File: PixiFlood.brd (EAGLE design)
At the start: 43 x 46 mm, 37 parts, among them IC1 TC7W04FP-0.65, IC2 WS2811S, IC3 78L05Z, U1 PT4115B89E, U2 PT4115B89E, U3 PT4115B89E, X1 22-23-2031, X2 22-23-2031

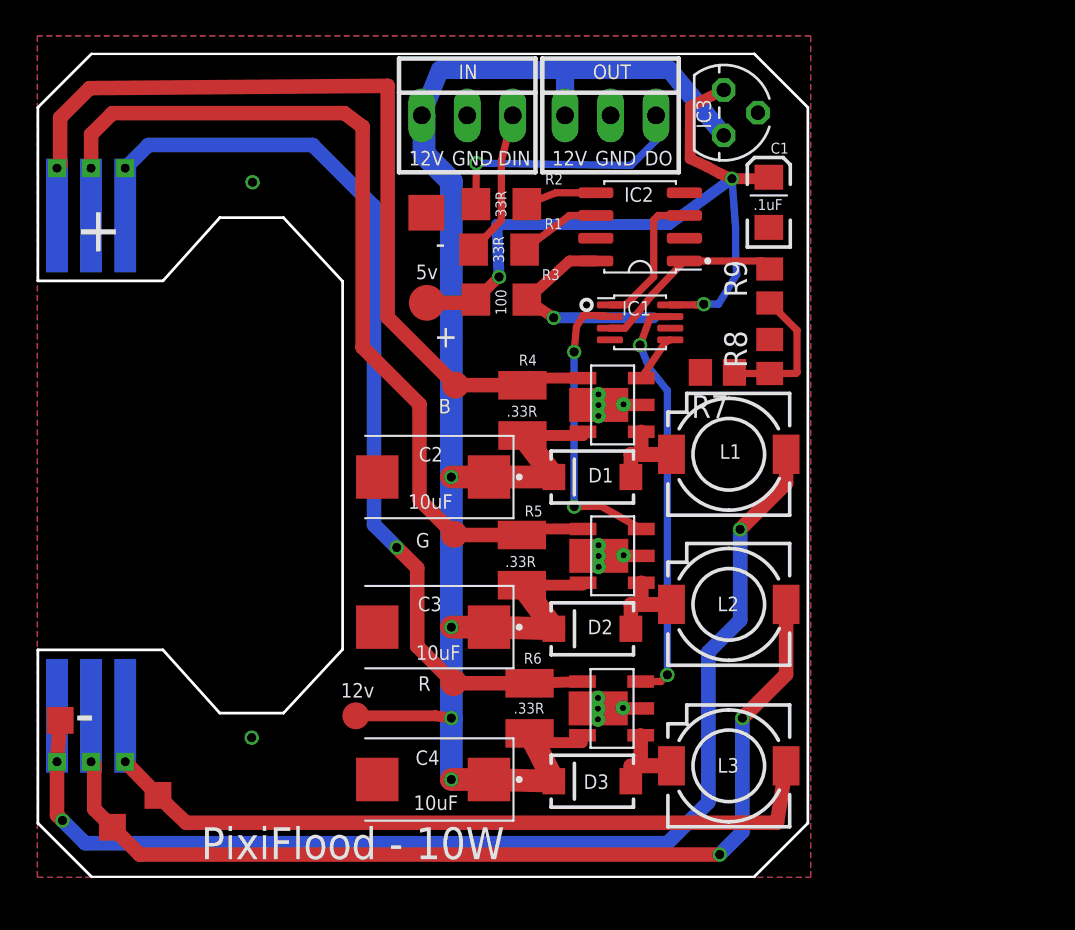
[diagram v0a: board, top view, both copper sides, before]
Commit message: Reworked layout
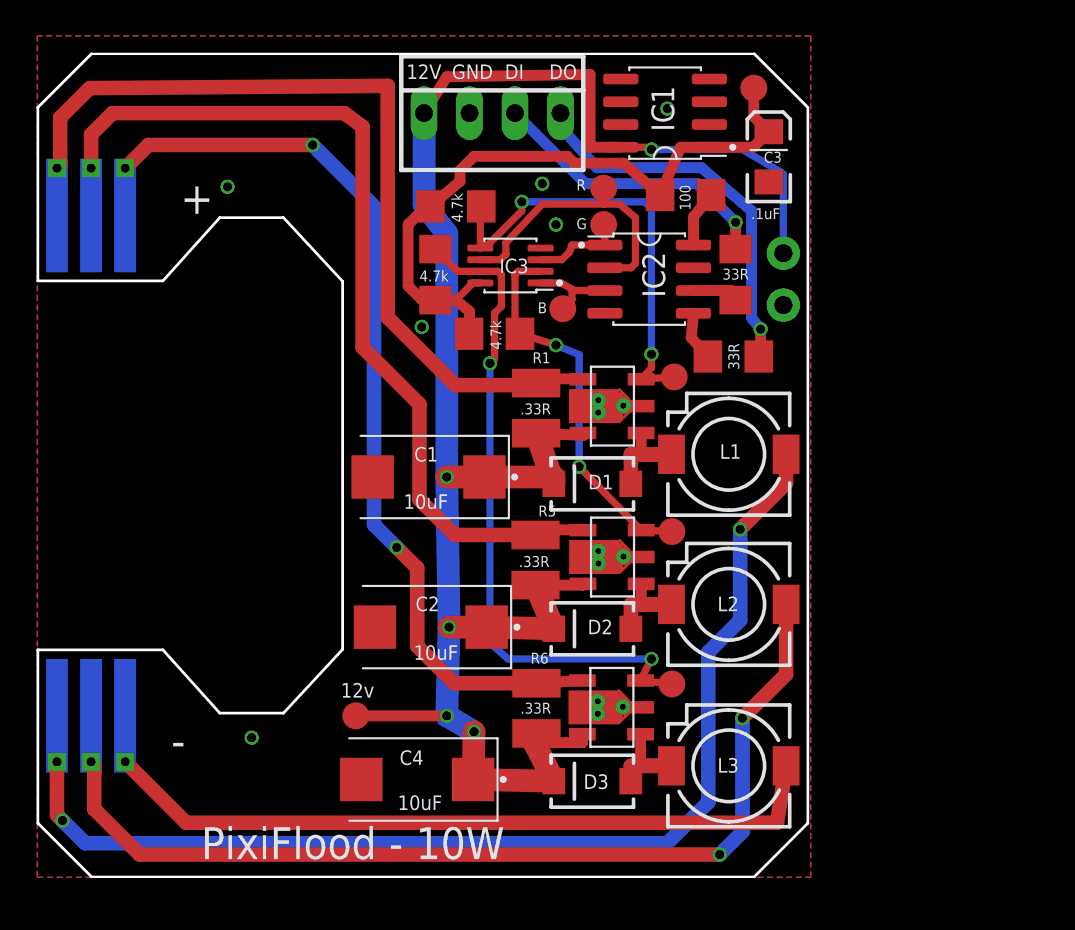
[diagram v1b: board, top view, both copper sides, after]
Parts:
- removed TP8: TPSQTP15SQ, testpad:TP15SQ
- removed X2: 22-23-2031, MyLibrary:22-23-2031
- added JP1: M02NO_SILK_LOCK, connectors:1X02_LOCK_NO_SILK
- C1: value .1uF -> 10uF; device capacitors:EIA3216 -> capacitors:VISHAY-CASE-D
- C3: value 10uF -> .1uF; device capacitors:VISHAY-CASE-D -> capacitors:EIA3216
- IC1: value TC7W04FP-0.65 -> 78L05SMD; device logic:SSOP8-0.65P -> regulators:SO08
- IC2: device drivers:WS2811S -> drivers:SO08
- IC3: value 78L05Z -> TC7W04FP-0.65; device linear:TO92 -> logic:SSOP8-0.65P
- R1: value 33R -> .33R; device rcl:R1206 -> resistor:R1210
- R3: value 100 -> 33R
- R4: value .33R -> 100; device resistor:R1210 -> rcl:R1206
- R7, R8, R9: value 4.7K -> 4.7k; device rcl:R0805 -> rcl:R1206
- TP1: value TPSQTP20R -> TPSQTP15R; device testpad:TP20R -> testpad:TP15R
- TP2: value TPSQTP20SQ -> TPSQTP15R; device testpad:TP20SQ -> testpad:TP15R
- TP4, TP6: value TPSQTP15SQ -> TPSQTP15R; device testpad:TP15SQ -> testpad:TP15R
- U1, U2, U3: value PT4115B89E -> PT4115B89E-A; device drivers:SOT89-5 -> drivers:SOT-89-5-A
- X1: value 22-23-2031 -> 22-23-2041; device MyLibrary:22-23-2031 -> connectors:22-23-2041
- moved TP6 35.3 mm to (35.4, 19.3)
- moved C3 32.3 mm to (40.8, 40.2), turned to 90 degrees
- moved TP5 30.0 mm to (40.0, 44.1)
- moved TP7 26.9 mm to (31.6, 36.4)
- moved C1 24.4 mm to (21.8, 22.4), turned to 0 degrees
- moved R9 18.1 mm to (23.4, 37.5), turned to 0 degrees
- moved TP9 17.7 mm to (35.4, 10.8)
- moved R7 16.7 mm to (22.2, 33.7), turned to 90 degrees
- moved TP4 16.5 mm to (17.8, 9.02)
- moved R8 15.4 mm to (25.5, 30.4), turned to 0 degrees
- moved R4 15.1 mm to (36.2, 38.1), turned to 0 degrees
- moved IC3 14.7 mm to (26.4, 34.2), turned to 90 degrees
- moved TP1 14.4 mm to (35.6, 27.9)
- moved TP3 13.8 mm to (31.6, 38.5)
- moved R2 13.7 mm to (39.0, 33.7), turned to 270 degrees
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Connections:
- removed net N$18: R7.1, R8.1, R9.1
- net +12V: now also C1.1, IC1.8, JP1.1, R1.2, TP4.TP; no longer C3.1, IC3.3, R4.2, TP9.TP, X2.1
- net +5V: now also C3.A, IC1.1, IC3.8, R4.1, R7.1, R8.1, R9.1, TP5.TP; no longer C1.A, IC1.8, IC3.1, R3.1, TP1.TP
- net BLUE: now also IC3.7, R7.2, TP9.TP; no longer IC1.7
- net BOUT: no longer TP7.TP
- net GND: now also C1.2, C3.C, IC1.2, IC1.3, IC1.6, IC1.7, IC3.4, JP1.2, U1.P$1, U1.P$2, U1.P$3, U1.P$4, U1.P$5, U2.P$1, U2.P$2, U2.P$3, U2.P$4, U2.P$5, U3.P$1, U3.P$2, U3.P$3, U3.P$4, U3.P$5; no longer C1.C, C3.2, IC1.4, IC3.2, TP2.TP, U1.2A@2, U2.2A@2, U3.2A@2, X2.2
- net GOUT: no longer TP5.TP
- net GREEN: now also IC3.2, R8.2, TP6.TP; no longer IC1.2
- net N$10: no longer TP8.TP
- net N$14: now also R4.2; no longer R3.2
- net N$15: now also IC3.3, TP7.TP; no longer IC1.3, R9.2
- net N$16: now also IC3.1, TP2.TP; no longer IC1.1, R7.2
- net N$19: now also IC3.6, TP3.TP; no longer IC1.6, R8.2
- net N$3: no longer TP4.TP
- net N$4: now also R3.1, X1.4; no longer R2.1, X2.3
- net N$6: now also R2.1; no longer R1.1
- net N$7: now also R3.2; no longer R2.2
- net N$8: now also R2.2; no longer R1.2
- net N$9: no longer TP6.TP
- net RED: now also IC3.5, R9.2, TP1.TP; no longer IC1.5
- net ROUT: now also R1.1; no longer R4.1, TP3.TP
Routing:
- net RED: track 2.72 -> 25.0 mm, vias 0 -> 2
- net N$19: track 0.00 -> 15.9 mm
- net BLUE: track 23.3 -> 37.6 mm
- net N$14: track 12.1 -> 3.14 mm, vias 1 -> 0
- net N$6: track 8.18 -> 16.3 mm, vias 0 -> 1
- net N$18: track 8.05 -> 0.00 mm
- net N$4: track 14.3 -> 21.7 mm
- net +12V: track 101.8 -> 107.7 mm, vias 4 -> 5
- net N$15: track 10.8 -> 5.34 mm
- net GREEN: track 16.4 -> 21.4 mm
- net N$16: track 8.09 -> 5.00 mm
- net +5V: track 41.2 -> 38.1 mm, vias 3 -> 0
- net N$3: track 67.1 -> 64.7 mm
- net N$8: track 4.62 -> 2.74 mm
- net N$7: track 3.97 -> 2.77 mm
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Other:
- board text added: "DI"
- board text added: "v1.8"
- board text removed: "+"
- board text removed: "-"
- board text removed: "5v"
- board text removed: "DIN"
- board text removed: "IN"
- board text removed: "OUT"
- board text removed: "v1.6"

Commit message: Reworked layout
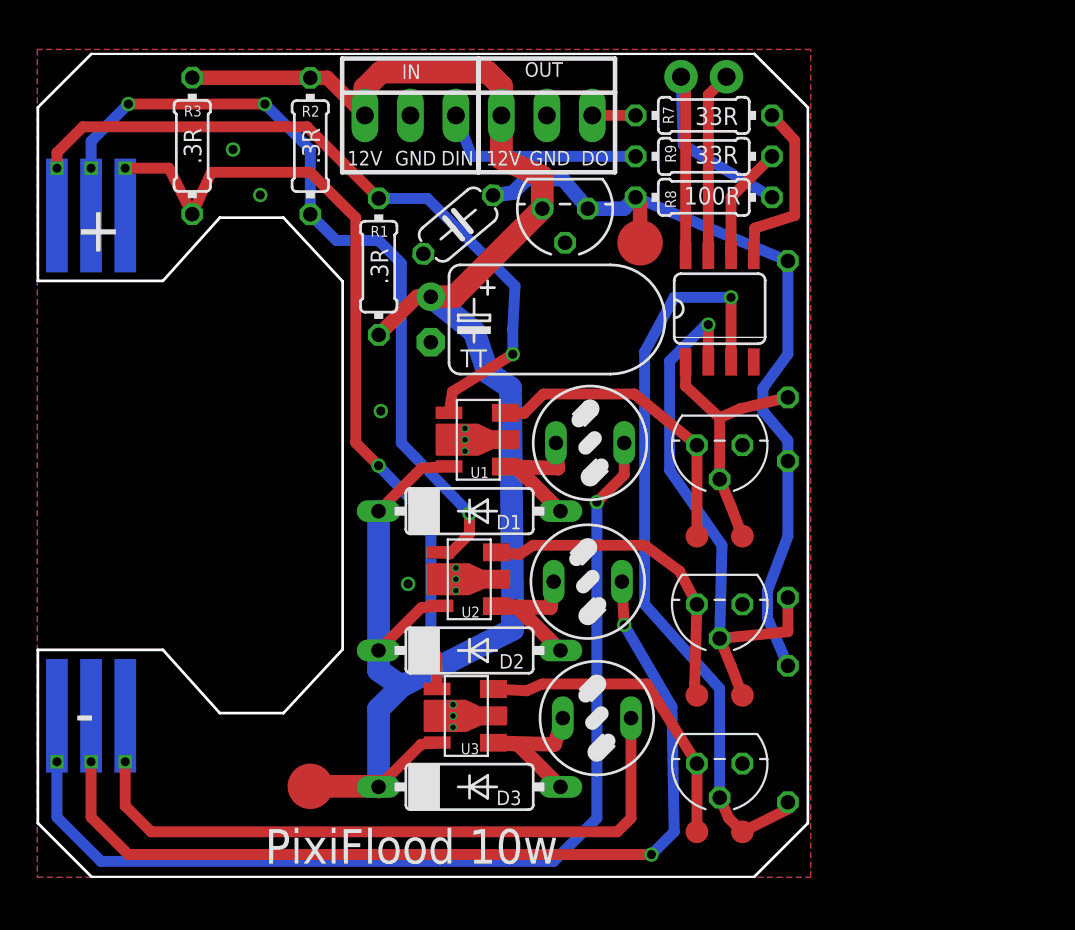
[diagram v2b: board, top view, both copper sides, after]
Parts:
- removed C3: .1uF, capacitors:EIA3216
- removed C4: 10uF, capacitors:VISHAY-CASE-D
- removed IC3: TC7W04FP-0.65, logic:SSOP8-0.65P
- removed TP9: TPSQTP15R, testpad:TP15R
- added T1, T2, T3: 2N3904, transistor:TO92
- added TP8: PTR1B1,27, testpad:B1,27
- added X2: 22-23-2031, connectors:22-23-2031
- C1: value 10uF -> 100uF; device capacitors:VISHAY-CASE-D -> rcl:TT2D6L
- C2: value 10uF -> .1uF; device capacitors:VISHAY-CASE-D -> rcl:C050-024X044
- D1, D2, D3: value B340A -> 2N3904; device SparkFun-DiscreteSemi:SMA-DIODE -> diode:DO07
- IC1: value 78L05SMD -> WS2811-SOP8; device regulators:SO08 -> MyLibrary:SO08-SKINNYPADS
- IC2: value WS2811S -> 78L05Z; device drivers:SO08 -> linear:TO92
- JP1: value M02NO_SILK_LOCK -> M021X02_NO_SILK; device connectors:1X02_LOCK_NO_SILK -> SparkFun-Connectors:1X02_NO_SILK
- L1, L2, L3: value SLF7045T-101MR60-H -> 82114R; device inductors:SLF7045 -> inductors:82114R
- R1: value .33R -> .3R; device resistor:R1210 -> resistor:0204/7
- R2, R3: value 33R -> .3R; device rcl:R1206 -> resistor:0204/7
- R4: value 100 -> 4.7k; device rcl:R1206 -> resistor:0204/7
- R5, R6: value .33R -> 4.7k; device resistor:R1210 -> resistor:0204/7
- R7, R9: value 4.7k -> 33R; device rcl:R1206 -> rcl:0204/7
- R8: value 4.7k -> 100R; device rcl:R1206 -> rcl:0204/7
- TP1, TP2: value TPSQTP15R -> PTR1B2,54; device testpad:TP15R -> testpad:B2,54
- TP3, TP4, TP5, TP6, TP7: value TPSQTP15R -> PTR1B1,27; device testpad:TP15R -> testpad:B1,27
- U1, U2, U3: value PT4115B89E-A -> PT4115B89E-A2; device drivers:SOT-89-5-A -> drivers:SOT89-5-A
- X1: value 22-23-2041 -> 22-23-2031; device connectors:22-23-2041 -> connectors:22-23-2031
- moved TP5 33.9 mm to (39.4, 10.2)
- moved R3 32.4 mm to (8.65, 40.8), turned to 270 degrees
- moved TP1 30.6 mm to (15.2, 5.08)
- moved TP7 26.8 mm to (36.8, 10.2)
- moved R2 24.8 mm to (15.2, 40.8)
- moved TP4 22.5 mm to (39.4, 2.54)
- moved C2 22.5 mm to (23.5, 36.4), turned to 220 degrees
- moved TP3 20.9 mm to (39.4, 19.1)
- moved R7 17.4 mm to (37.2, 42.5), turned to 0 degrees
- moved R5 14.2 mm to (41.9, 19.4), flipped to the bottom
- moved R9 14.1 mm to (37.2, 40.3)
- moved R6 14.1 mm to (41.9, 8.00), flipped to the bottom
- moved R8 13.9 mm to (37.2, 38.0)
- moved R1 11.8 mm to (19.1, 34.1), turned to 90 degrees
- moved JP1 11.5 mm to (35.9, 44.7), turned to 0 degrees
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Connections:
- removed net N$14: IC2.8, R4.2
- removed net N$19: IC2.2, IC3.6, TP3.TP
- new net N$18: IC1.2, R5.2, T2.2, TP5.TP
- new net N$20: IC1.1, R4.2, T1.2, TP3.TP
- new net VDD: IC1.8, JP1.1, R8.2
- net +12V: now also C1.+, IC2.3, R1.1, R2.1, R3.1, TP1.TP, X2.1; no longer C1.1, C2.1, C4.1, IC1.8, JP1.1, R1.2, R5.2, R6.2, TP4.TP
- net +5V: now also C2.1, IC2.1, R5.1, R6.1, TP2.TP; no longer C3.A, IC1.1, IC3.8, R7.1, R9.1, TP5.TP
- net BLUE: now also T3.1, TP8.TP; no longer IC3.7, R7.2, TP9.TP
- net BOUT: now also R3.2; no longer R6.1
- net GND: now also C1.-, IC1.4, IC2.2, T1.3, T2.3, T3.3, U1.2@1, U1.2@2, U1.2@3, U2.2@1, U2.2@2, U2.2@3, U3.2@1, U3.2@2, U3.2@3, X2.2; no longer C1.2, C3.C, C4.2, IC1.2, IC1.3, IC1.6, IC1.7, IC2.4, IC3.4, JP1.2, U1.2A, U1.2A@1, U1.2A@3, U1.2A@4, U1.P$1, U1.P$2, U1.P$3, U1.P$4, U1.P$5, U2.2A, U2.2A@1, U2.2A@3, U2.2A@4, U2.P$1, U2.P$2, U2.P$3, U2.P$4, U2.P$5, U3.2A, U3.2A@1, U3.2A@3, U3.2A@4, U3.P$1, U3.P$2, U3.P$3, U3.P$4, U3.P$5
- net GOUT: now also R2.2; no longer R5.1
- net GREEN: now also T2.1, TP7.TP; no longer IC3.2, R8.2, TP6.TP
- net N$15: now also IC1.3, R6.2, T3.2, TP4.TP; no longer IC2.1, IC3.3, TP7.TP
- net N$16: now also IC1.7, JP1.2; no longer IC2.3, IC3.1, TP2.TP
- net N$4: now also R7.1, X1.3; no longer R3.1, X1.4
- net N$6: now also R9.1, X2.3; no longer R2.1, X1.3
- net N$7: now also IC1.5, R7.2; no longer IC2.5, R3.2
- net N$8: now also IC1.6, R9.2; no longer IC2.6, R2.2
- net RED: now also T1.1, TP6.TP; no longer IC3.5, R9.2, TP1.TP
- net ROUT: now also R1.2; no longer R1.1
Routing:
- net N$15: track 5.34 -> 42.3 mm, vias 0 -> 1
- net N$18: track 0.00 -> 30.7 mm, vias 0 -> 1
- net BLUE: track 37.6 -> 17.7 mm, vias 2 -> 0
- net VDD: track 0.00 -> 19.6 mm
- net N$4: track 21.7 -> 2.41 mm, vias 1 -> 0
- net N$19: track 15.9 -> 0.00 mm
- net N$20: track 0.00 -> 14.8 mm
- net ROUT: track 50.7 -> 42.3 mm, vias 0 -> 1
- net RED: track 25.0 -> 17.2 mm, vias 2 -> 0
- net N$7: track 2.77 -> 9.95 mm
- net +5V: track 38.1 -> 45.2 mm
- net GOUT: track 53.5 -> 46.9 mm, vias 0 -> 3
- net BOUT: track 54.1 -> 47.7 mm
- net N$16: track 5.00 -> 10.4 mm
- net +12V: track 107.7 -> 102.3 mm, vias 5 -> 0
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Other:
- board text added: "DIN"
- board text added: "IN"
- board text added: "OUT"
- board text added: "PixiFlood 10w"
- board text added: "V1.9a"
- board text removed: "12v"
- board text removed: "B"
- board text removed: "DI"
- board text removed: "G"
- board text removed: "PixiFlood - 10W"
- board text removed: "R"
- board text removed: "v1.8"

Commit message: Reworked layout
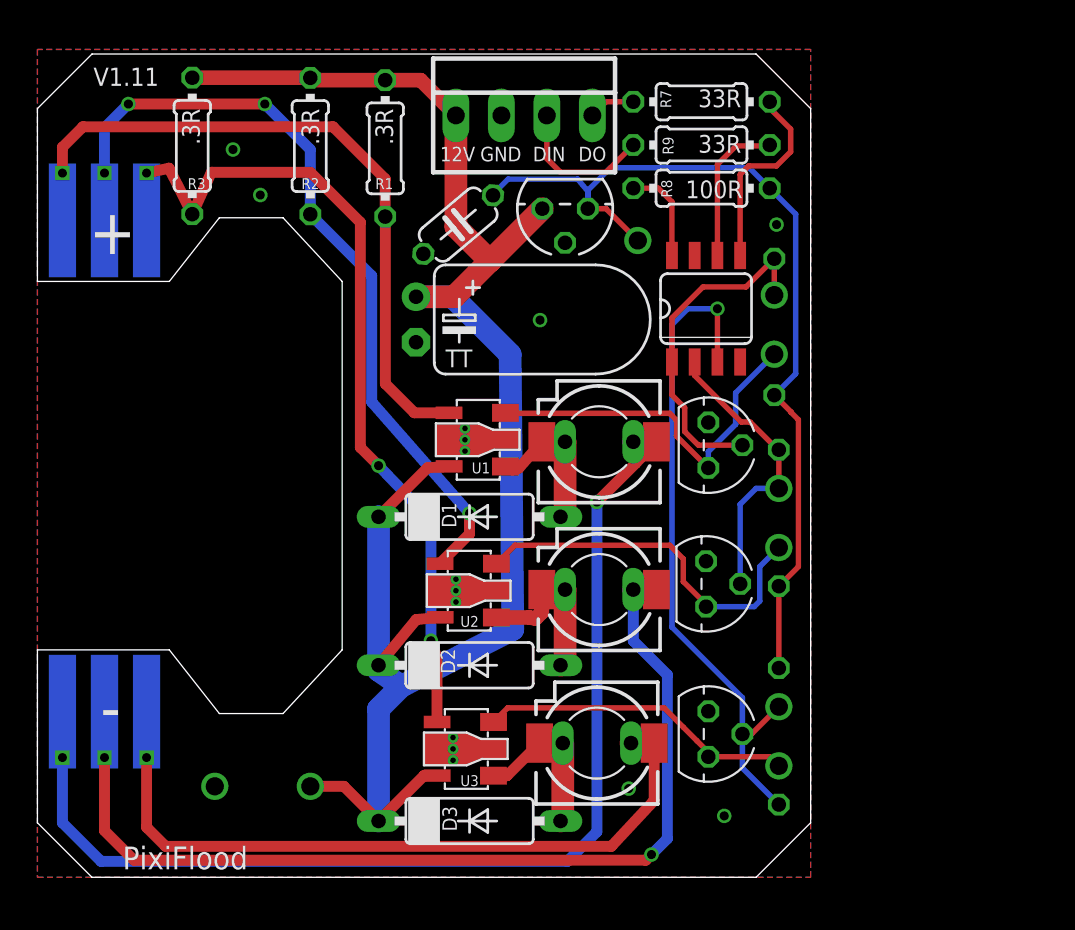
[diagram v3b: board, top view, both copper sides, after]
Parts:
- removed JP1: M021X02_NO_SILK, SparkFun-Connectors:1X02_NO_SILK
- removed TP1, TP2: PTR1B2,54, testpad:B2,54
- removed TP3, TP4, TP5, TP6, TP7, TP8: PTR1B1,27, testpad:B1,27
- removed X1: 22-23-2031, connectors:22-23-2031
- added T$1, T$2, T$3, T$4, T$5, T$6, T$7, T$8, T$9: TEST_PINTP-2, headers:TP-2
- B1: value LED-BOARDV4 -> LED-BOARDNODIM; device special:LED_BOARD-V4 -> myBoards:LED_BOARD_V5_A
- D1, D2, D3: value 2N3904 -> 1N5819
- L1, L2, L3: value 82114R -> INDUCTOR82114R; device inductors:82114R -> rcl:82114R-C
- U1, U2, U3: value PT4115B89E-A2 -> PT4115B89E; device drivers:SOT89-5-A -> drivers:SOT89-5
- X2: value 22-23-2031 -> 22-23-2041; device connectors:22-23-2031 -> connectors:22-23-2041
- moved R1 6.62 mm to (19.4, 40.7), turned to 270 degrees
- moved X2 6.35 mm to (27.2, 42.5)
- moved D3 1.91 mm to (24.1, 3.14)
- moved U3 1.84 mm to (24.0, 7.17)
- moved T3 1.77 mm to (37.5, 8.00), turned to 270 degrees
- moved L3 1.40 mm to (31.2, 7.49), turned to 270 degrees
- moved T2 1.37 mm to (37.3, 16.4), turned to 270 degrees
- moved C1 0.83 mm to (21.1, 31.1)
- moved D2 0.83 mm to (24.1, 11.8)
- moved R5 0.81 mm to (41.4, 20.1), turned to 90 degrees
- moved L2 0.78 mm to (31.4, 16.1), turned to 270 degrees
- moved R7 0.77 mm to (37.1, 43.3)
- moved R4 0.77 mm to (41.1, 30.7), turned to 90 degrees
- moved IC1 0.76 mm to (37.3, 31.8)
- moved R9 0.65 mm to (37.1, 40.9)
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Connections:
- net N$6 renamed DIN
- net N$7 renamed DO-R
- net N$8 renamed DIN-R
- removed net N$16: IC1.7, JP1.2
- removed net N$4: R7.1, X1.3
- new net DO: R7.1, X2.4
- net +12V: now also T$9.P$1; no longer TP1.TP, X1.1
- net +5V: now also T$2.P$1; no longer TP2.TP
- net BLUE: now also T$6.P$1; no longer TP8.TP
- net GND: now also T$3.P$1; no longer X1.2
- net GREEN: now also T$7.P$1; no longer TP7.TP
- net N$1: now also L1.1@A
- net N$10: now also L3.2@A
- net N$15: now also T$5.P$1; no longer TP4.TP
- net N$18: now also T$4.P$1; no longer TP5.TP
- net N$2: now also L3.1@A
- net N$20: now also T$1.P$1; no longer TP3.TP
- net N$3: now also L1.2@A
- net N$5: now also L2.1@A
- net N$9: now also L2.2@A
- net RED: now also T$8.P$1; no longer TP6.TP
- net VDD: no longer JP1.1
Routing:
- net N$18: track 30.7 -> 16.3 mm, vias 1 -> 0
- net VDD: track 19.6 -> 5.47 mm
- net N$16: track 10.4 -> 0.00 mm
- net +5V: track 45.2 -> 51.6 mm
- net N$3: track 59.4 -> 64.6 mm
- net N$20: track 14.8 -> 19.3 mm
- net N$15: track 42.3 -> 37.8 mm
- net RED: track 17.2 -> 21.0 mm
- net DIN: track 11.6 -> 8.19 mm
- net +12V: track 102.3 -> 99.4 mm
- net GREEN: track 18.1 -> 20.9 mm
- net ROUT: track 42.3 -> 39.7 mm, vias 1 -> 0
- net DO: track 0.00 -> 2.60 mm
- net N$4: track 2.41 -> 0.00 mm
- net DIN-R: track 6.48 -> 8.46 mm
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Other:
- board size 43 x 46 mm -> 43.2 x 46 mm
- board text added: "PixiFlood"
- board text added: "V1.11"
- board text removed: "IN"
- board text removed: "OUT"
- board text removed: "PixiFlood 10w"
- board text removed: "V1.9a"
